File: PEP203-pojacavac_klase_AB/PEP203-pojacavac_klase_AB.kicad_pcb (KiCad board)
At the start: 2 copper layers, 45 x 45 mm, 31 parts, among them J1 Screw_Terminal_01x02, J2 Conn_01x02_Pin, J3 Conn_01x02_Pin, J4 Conn_01x02_Pin, J5 Conn_01x02_Pin, J6 Conn_01x02_Pin, Q2 MMBT5551L, Q3 MMBT5401

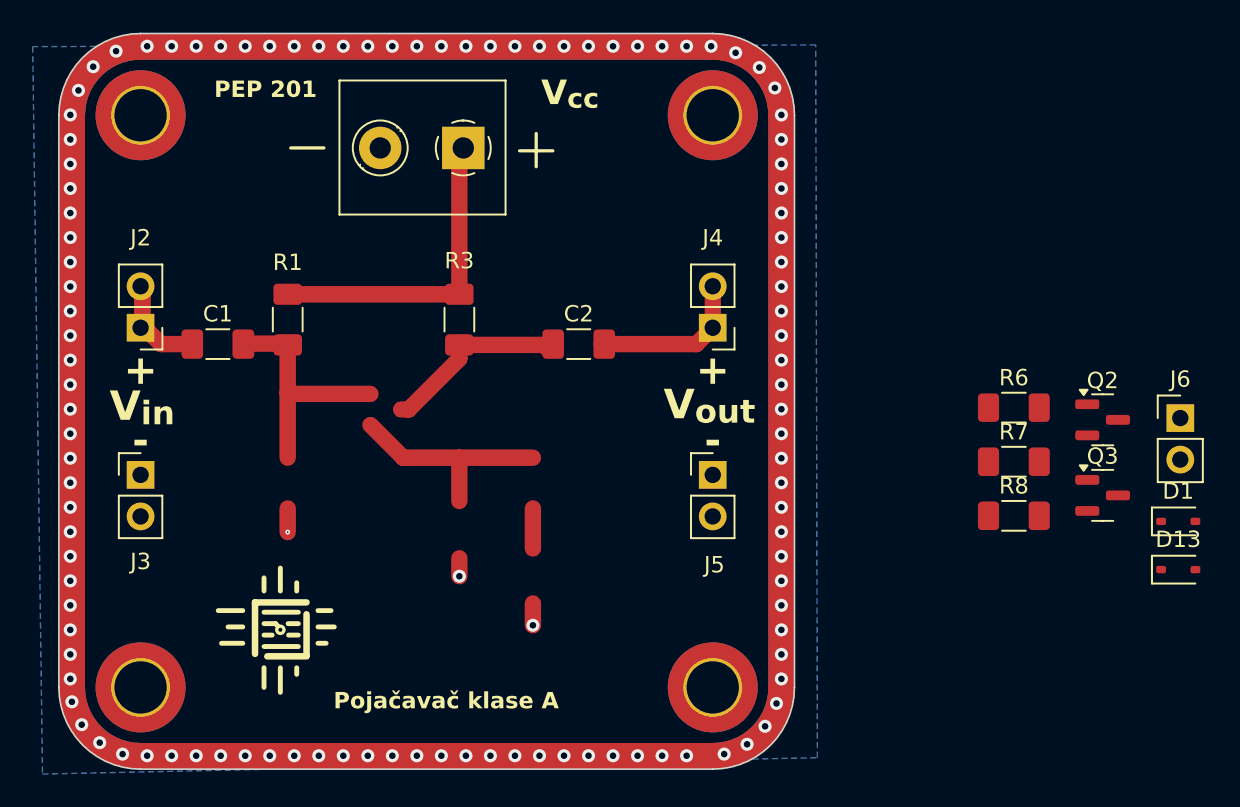
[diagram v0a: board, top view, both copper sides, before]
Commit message: Added class AB.
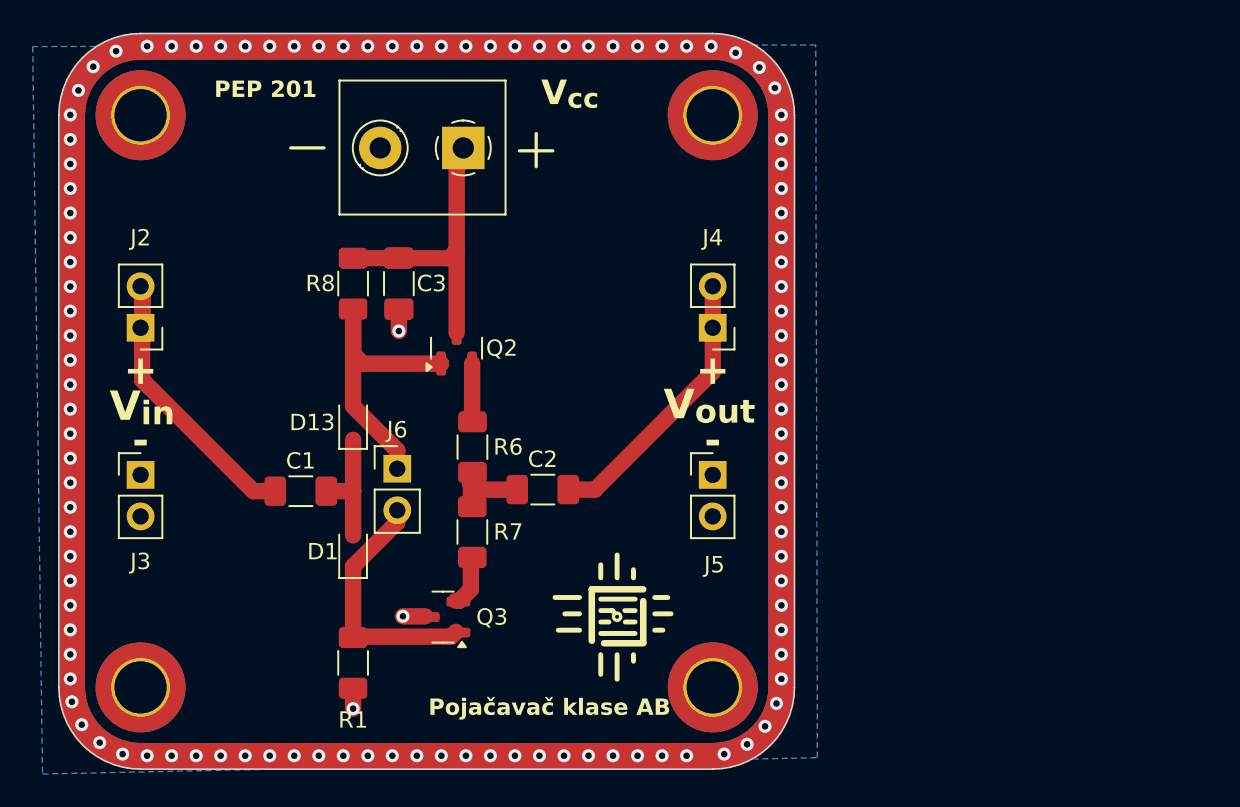
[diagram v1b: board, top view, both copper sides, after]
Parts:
- removed the ? at (123.4, 108.5)
- removed the ? at (131.6, 118.1)
- removed the ? at (116.9, 109.8)
- removed the ? at (116.9, 123.0)
- removed the ? at (130.0, 125.3)
- removed the ? at (123.5, 123.0)
- removed the ? at (130.0, 124.2)
- removed R3: 10k, Resistor_SMD:R_1206_3216Metric_Pad1.30x1.75mm_HandSolder
- added ?: , clipboard:f3223f44-050f-45ab-bded-9586cede3436, F.Cu at (130.9, 128.0)
- added C3: 10u, Capacitor_SMD:C_1206_3216Metric_Pad1.33x1.80mm_HandSolder, F.Cu at (120.8, 115.3)
- added REF**: diode_silk, PEP_library:diode_silk, F.Cu at (118.0, 123.8)
- added REF**: R_silk_symbol, PEP_library:R_silk_symbol, F.Cu at (124.6, 128.0)
- added REF**: R_silk_symbol, PEP_library:R_silk_symbol, F.Cu at (118.0, 135.5)
- added REF**: R_silk_symbol, PEP_library:R_silk_symbol, F.Cu at (118.0, 112.3)
- added REF**: diode_silk, PEP_library:diode_silk, F.Cu at (118.0, 131.7)
- added REF**: PNP_silk, PEP_library:PNP_silk, F.Cu at (121.8, 135.6)
- added REF**: R_silk_symbol, PEP_library:R_silk_symbol, F.Cu at (124.6, 121.9)
- moved D13 51.3 mm to (118.0, 123.8), turned to 90 degrees
- moved D1 50.5 mm to (118.0, 131.7), turned to 90 degrees
- moved J6 48.0 mm to (120.7, 126.6)
- moved R8 42.8 mm to (118.0, 115.3), turned to -90 degrees
- moved Q3 41.0 mm to (123.5, 135.7), turned to 180 degrees
- moved Q2 39.8 mm to (124.3, 119.2), turned to 90 degrees
- moved R7 33.4 mm to (125.3, 130.5), turned to -90 degrees
- moved R6 33.2 mm to (125.3, 125.3), turned to -90 degrees
- moved R1 21.4 mm to (118.0, 138.5), turned to -90 degrees
- moved REF** 20.6 mm to (134.2, 135.7)
- moved C1 10.3 mm to (114.8, 128.0)
- moved C2 9.17 mm to (129.6, 127.9)
- moved ? 7.43 mm to (117.0, 128.0)
- moved REF** 2.15 mm to (122.9, 119.3)
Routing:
- net (no net): track 30.7 -> 0.00 mm
- net Net-(D13-A): track 0.00 -> 19.4 mm
- net Net-(D1-K): track 0.00 -> 15.4 mm
- net Net-(Q1-C): track 12.1 -> 0.00 mm
- net V_{in}: track 7.24 -> 18.2 mm
- net Net-(D1-A): track 0.00 -> 7.49 mm
- net V_{out}: track 9.70 -> 17.1 mm
- net Net-(C2-Pad1): track 0.00 -> 5.06 mm
- net Net-(Q2-E): track 0.00 -> 3.42 mm
- net Net-(Q3-E): track 0.00 -> 3.35 mm
- net Vcc: track 19.9 -> 19.3 mm
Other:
- board text added: "Pojačavač klase AB"
- board text removed: "C_{1}"
- board text removed: "C_{2}"
- board text removed: "C_{3}"
- board text removed: "Pojačavač klase A"
- board text removed: "R_{1}"
- board text removed: "R_{2}"
- board text removed: "R_{3}"
- board text removed: "R_{4}"
- board text removed: "R_{5}"
